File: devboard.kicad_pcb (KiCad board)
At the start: 2 copper layers, 0 parts

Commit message: Exploration into bus layout
This commit made to save progress before attempting new layout.
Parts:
- added C1: 100n, Capacitor_SMD:C_0603_1608Metric_Pad1.08x0.95mm_HandSolder, F.Cu at (166.4, 105.4)
- added C10: 10u, Capacitor_SMD:C_0603_1608Metric_Pad1.08x0.95mm_HandSolder, F.Cu at (187.1, 76.6)
- added C11: 100n, Capacitor_SMD:C_0603_1608Metric_Pad1.08x0.95mm_HandSolder, F.Cu at (43.2, 31.3)
- added C12: 100n, Capacitor_SMD:C_0603_1608Metric_Pad1.08x0.95mm_HandSolder, F.Cu at (268.0, 146.3)
- added C13: 100n, Capacitor_SMD:C_0603_1608Metric_Pad1.08x0.95mm_HandSolder, F.Cu at (61.6, 32.2)
- added C14: 100n, Capacitor_SMD:C_0603_1608Metric_Pad1.08x0.95mm_HandSolder, F.Cu at (287.0, 146.9)
- added C15: 100n, Capacitor_SMD:C_0603_1608Metric_Pad1.08x0.95mm_HandSolder, F.Cu at (68.6, 31.3)
- added C16: 100n, Capacitor_SMD:C_0603_1608Metric_Pad1.08x0.95mm_HandSolder, F.Cu at (293.4, 146.3)
- added C17: 100n, Capacitor_SMD:C_0603_1608Metric_Pad1.08x0.95mm_HandSolder, F.Cu at (87.0, 32.2)
- added C18: 100n, Capacitor_SMD:C_0603_1608Metric_Pad1.08x0.95mm_HandSolder, F.Cu at (312.4, 146.7)
- added C19: 100n, Capacitor_SMD:C_0603_1608Metric_Pad1.08x0.95mm_HandSolder, F.Cu at (92.7, 31.5)
- added C2: 100n, Capacitor_SMD:C_0603_1608Metric_Pad1.08x0.95mm_HandSolder, F.Cu at (144.8, 123.7)
- added C20: 100n, Capacitor_SMD:C_0603_1608Metric_Pad1.08x0.95mm_HandSolder, F.Cu at (318.1, 146.7)
- added C21: 100n, Capacitor_SMD:C_0603_1608Metric_Pad1.08x0.95mm_HandSolder, F.Cu at (111.8, 32.2)
- added C22: 100n, Capacitor_SMD:C_0603_1608Metric_Pad1.08x0.95mm_HandSolder, F.Cu at (337.2, 146.7)
- added C23: 100n, Capacitor_SMD:C_0603_1608Metric_Pad1.08x0.95mm_HandSolder, F.Cu at (188.1, 91.6)
- added C24: 10u, Capacitor_SMD:C_0603_1608Metric_Pad1.08x0.95mm_HandSolder, F.Cu at (183.7, 96.3)
- added C25: 10n, Capacitor_SMD:C_0603_1608Metric_Pad1.08x0.95mm_HandSolder, F.Cu at (170.7, 108.4)
- added C26: 100n, Capacitor_SMD:C_0603_1608Metric_Pad1.08x0.95mm_HandSolder, F.Cu at (144.8, 121.2)
- added C27: 100n, Capacitor_SMD:C_0603_1608Metric_Pad1.08x0.95mm_HandSolder, F.Cu at (154.0, 118.5)
- added C28: 100n, Capacitor_SMD:C_0603_1608Metric_Pad1.08x0.95mm_HandSolder, F.Cu at (183.7, 88.7)
- added C3: 100n, Capacitor_SMD:C_0603_1608Metric_Pad1.08x0.95mm_HandSolder, F.Cu at (149.1, 121.2)
- added C4: 100n, Capacitor_SMD:C_0603_1608Metric_Pad1.08x0.95mm_HandSolder, F.Cu at (186.8, 81.6)
- added C5: 1u, Capacitor_SMD:C_0603_1608Metric_Pad1.08x0.95mm_HandSolder, F.Cu at (158.8, 81.9)
- added C6: 1u, Capacitor_SMD:C_0603_1608Metric_Pad1.08x0.95mm_HandSolder, F.Cu at (157.0, 109.8)
- added C7: 100n, Capacitor_SMD:C_0603_1608Metric_Pad1.08x0.95mm_HandSolder, F.Cu at (183.7, 86.2)
- added C8: 10u, Capacitor_SMD:C_0603_1608Metric_Pad1.08x0.95mm_HandSolder, F.Cu at (157.0, 107.3)
- added C9: 10u, Capacitor_SMD:C_0603_1608Metric_Pad1.08x0.95mm_HandSolder, F.Cu at (187.1, 79.1)
- added D1: 3.3 VRW, Diode_SMD:D_SOD-923, F.Cu at (191.6, 89.9)
- added D10: 3.3 VRW, Diode_SMD:D_SOD-923, F.Cu at (190.7, 76.3)
- added D2: RXLED, LED_SMD:LED_0603_1608Metric_Castellated, F.Cu at (104.8, 124.0)
- added D3: 3.3 VRW, Diode_SMD:D_SOD-923, F.Cu at (191.6, 88.0)
- added D4: 3.3 VRW, Diode_SMD:D_SOD-923, F.Cu at (191.6, 86.0)
- added D5: TXLED, LED_SMD:LED_0603_1608Metric_Castellated, F.Cu at (112.0, 101.3)
- added D6: 3.3 VRW, Diode_SMD:D_SOD-923, F.Cu at (191.6, 84.1)
- added D7: 3.3 VRW, Diode_SMD:D_SOD-923, F.Cu at (191.6, 82.1)
- added D8: 3.3 VRW, Diode_SMD:D_SOD-923, F.Cu at (190.7, 80.2)
- added D9: 3.3 VRW, Diode_SMD:D_SOD-923, F.Cu at (190.7, 78.2)
- added FB1: 500mA, Inductor_SMD:L_0603_1608Metric_Pad1.05x0.95mm_HandSolder, F.Cu at (171.0, 100.9)
- added J1: Conn_01x04, Connector_PinHeader_2.54mm:PinHeader_1x04_P2.54mm_Vertical, F.Cu at (147.7, 97.6)
- added J2: Conn_02x05_Odd_Even, Connector_PinHeader_1.27mm:PinHeader_2x05_P1.27mm_Vertical, F.Cu at (129.9, 116.9)
- added J3: USB_B_Micro, Connector_USB:USB_Micro-B_Wuerth_629105150521, F.Cu at (69.8, 163.8)
- added J4: Conn_01x04, Connector_PinHeader_2.54mm:PinHeader_1x04_P2.54mm_Vertical, F.Cu at (173.3, 77.6)
- added J5: Conn_02x10_Counter_Clockwise, Connector_PinHeader_2.54mm:PinHeader_2x10_P2.54mm_Vertical, F.Cu at (19.1, 66.0)
- added J6: Conn_02x04_Counter_Clockwise, Connector_PinHeader_2.54mm:PinHeader_2x04_P2.54mm_Vertical, F.Cu at (154.9, 96.1)
- added Q1: Q_NPN_BEC, Package_TO_SOT_SMD:SOT-23, F.Cu at (162.0, 105.3)
- added Q2: Q_NPN_BEC, Package_TO_SOT_SMD:SOT-23, F.Cu at (166.6, 101.9)
- added R1: 330, Resistor_SMD:R_0603_1608Metric_Pad0.98x0.95mm_HandSolder, F.Cu at (161.4, 108.9)
- added R10: 40k, Resistor_SMD:R_0603_1608Metric_Pad0.98x0.95mm_HandSolder, F.Cu at (269.9, 149.9)
- added R11: 1k, Resistor_SMD:R_0603_1608Metric_Pad0.98x0.95mm_HandSolder, F.Cu at (162.7, 121.4)
- added R12: 40k, Resistor_SMD:R_0603_1608Metric_Pad0.98x0.95mm_HandSolder, F.Cu at (269.9, 142.6)
- added R13: 40k, Resistor_SMD:R_0603_1608Metric_Pad0.98x0.95mm_HandSolder, F.Cu at (87.0, 24.5)
- added R14: 40k, Resistor_SMD:R_0603_1608Metric_Pad0.98x0.95mm_HandSolder, F.Cu at (312.4, 139.1)
- added R15: 40k, Resistor_SMD:R_0603_1608Metric_Pad0.98x0.95mm_HandSolder, F.Cu at (70.5, 34.9)
- added R16: 40k, Resistor_SMD:R_0603_1608Metric_Pad0.98x0.95mm_HandSolder, F.Cu at (295.3, 149.9)
- added R17: 40k, Resistor_SMD:R_0603_1608Metric_Pad0.98x0.95mm_HandSolder, F.Cu at (61.6, 28.3)
- added R18: 40k, Resistor_SMD:R_0603_1608Metric_Pad0.98x0.95mm_HandSolder, F.Cu at (287.0, 143.2)
- added R19: 40k, Resistor_SMD:R_0603_1608Metric_Pad0.98x0.95mm_HandSolder, F.Cu at (111.8, 24.5)
- added R2: 10k, Resistor_SMD:R_0603_1608Metric_Pad0.98x0.95mm_HandSolder, F.Cu at (149.6, 118.5)
- added R20: 40k, Resistor_SMD:R_0603_1608Metric_Pad0.98x0.95mm_HandSolder, F.Cu at (337.2, 139.1)
- added R21: 40k, Resistor_SMD:R_0603_1608Metric_Pad0.98x0.95mm_HandSolder, F.Cu at (94.6, 35.2)
- added R22: 40k, Resistor_SMD:R_0603_1608Metric_Pad0.98x0.95mm_HandSolder, F.Cu at (320.0, 150.1)
- added R23: 40k, Resistor_SMD:R_0603_1608Metric_Pad0.98x0.95mm_HandSolder, F.Cu at (70.5, 27.6)
- added R24: 40k, Resistor_SMD:R_0603_1608Metric_Pad0.98x0.95mm_HandSolder, F.Cu at (295.3, 142.6)
- added R25: 40k, Resistor_SMD:R_0603_1608Metric_Pad0.98x0.95mm_HandSolder, F.Cu at (87.0, 28.2)
- added R26: 40k, Resistor_SMD:R_0603_1608Metric_Pad0.98x0.95mm_HandSolder, F.Cu at (312.4, 142.9)
- added R27: 40k, Resistor_SMD:R_0603_1608Metric_Pad0.98x0.95mm_HandSolder, F.Cu at (94.6, 27.6)
- added R28: 40k, Resistor_SMD:R_0603_1608Metric_Pad0.98x0.95mm_HandSolder, F.Cu at (320.0, 142.9)
- added R29: 40k, Resistor_SMD:R_0603_1608Metric_Pad0.98x0.95mm_HandSolder, F.Cu at (111.8, 28.3)
- added R3: 10k, Resistor_SMD:R_0603_1608Metric_Pad0.98x0.95mm_HandSolder, F.Cu at (154.0, 115.9)
- added R30: 40k, Resistor_SMD:R_0603_1608Metric_Pad0.98x0.95mm_HandSolder, F.Cu at (337.2, 142.9)
- added R31: 4.7k, Resistor_SMD:R_0603_1608Metric_Pad0.98x0.95mm_HandSolder, F.Cu at (109.2, 124.0)
- added R32: 4.7k, Resistor_SMD:R_0603_1608Metric_Pad0.98x0.95mm_HandSolder, F.Cu at (167.0, 112.9)
- added R4: 10k, Resistor_SMD:R_0603_1608Metric_Pad0.98x0.95mm_HandSolder, F.Cu at (157.8, 122.3)
- added R5: 40k, Resistor_SMD:R_0603_1608Metric_Pad0.98x0.95mm_HandSolder, F.Cu at (45.1, 27.6)
- added R6: 1k, Resistor_SMD:R_0603_1608Metric_Pad0.98x0.95mm_HandSolder, F.Cu at (167.0, 115.5)
- added R7: 40k, Resistor_SMD:R_0603_1608Metric_Pad0.98x0.95mm_HandSolder, F.Cu at (61.6, 24.5)
- added R8: 40k, Resistor_SMD:R_0603_1608Metric_Pad0.98x0.95mm_HandSolder, F.Cu at (287.0, 139.4)
- added R9: 40k, Resistor_SMD:R_0603_1608Metric_Pad0.98x0.95mm_HandSolder, F.Cu at (45.1, 34.9)
- added SW1: SW_SPST, Button_Switch_SMD:SW_SPST_PTS810, F.Cu at (113.2, 97.7)
- added TP1: TestPoint, Connector_PinHeader_2.54mm:PinHeader_1x01_P2.54mm_Vertical, F.Cu at (135.6, 122.2)
- added TP10: TestPoint, Connector_PinHeader_2.54mm:PinHeader_1x01_P2.54mm_Vertical, F.Cu at (152.5, 108.3)
- added TP11: TestPoint, Connector_PinHeader_2.54mm:PinHeader_1x01_P2.54mm_Vertical, F.Cu at (178.0, 77.6)
- added TP2: TestPoint, Connector_PinHeader_2.54mm:PinHeader_1x01_P2.54mm_Vertical, F.Cu at (166.7, 96.1)
- added TP3: TestPoint, Connector_PinHeader_2.54mm:PinHeader_1x01_P2.54mm_Vertical, F.Cu at (145.1, 117.6)
- added TP4: TestPoint, Connector_PinHeader_2.54mm:PinHeader_1x01_P2.54mm_Vertical, F.Cu at (162.1, 100.7)
- added TP5: TestPoint, Connector_PinHeader_2.54mm:PinHeader_1x01_P2.54mm_Vertical, F.Cu at (162.1, 96.1)
- added TP6: TestPoint, Connector_PinHeader_2.54mm:PinHeader_1x01_P2.54mm_Vertical, F.Cu at (182.6, 77.6)
- added TP7: TestPoint, Connector_PinHeader_2.54mm:PinHeader_1x01_P2.54mm_Vertical, F.Cu at (140.3, 122.2)
- added TP8: TestPoint, Connector_PinHeader_2.54mm:PinHeader_1x01_P2.54mm_Vertical, F.Cu at (178.0, 82.3)
- added TP9: TestPoint, Connector_PinHeader_2.54mm:PinHeader_1x01_P2.54mm_Vertical, F.Cu at (140.5, 117.6)
- added U1: ATmega128L-8AU, Package_QFP:TQFP-64_14x14mm_P0.8mm, F.Cu at (128.9, 44.5)
- added U10: FT232RL, Package_SO:SSOP-28_5.3x10.2mm_P0.65mm, F.Cu at (69.8, 154.9)
- added U2: MAX6371, Package_TO_SOT_SMD:SOT-23-8, F.Cu at (147.8, 109.8)
- added U3: CY62158EV30LL-45ZSXIT, Package_SO:TSOP-II-44_10.16x18.41mm_P0.8mm, F.Cu at (278.6, 146.8)
- added U4: AP2112K-3.3, Package_TO_SOT_SMD:SOT-23-5, F.Cu at (135.7, 117.6)
- added U5: CY62158EV30LL-45ZSXIT, Package_SO:TSOP-II-44_10.16x18.41mm_P0.8mm, F.Cu at (53.5, 31.7)
- added U6: CY62158EV30LL-45ZSXIT, Package_SO:TSOP-II-44_10.16x18.41mm_P0.8mm, F.Cu at (78.7, 31.8)
- added U7: CY62158EV30LL-45ZSXIT, Package_SO:TSOP-II-44_10.16x18.41mm_P0.8mm, F.Cu at (304.2, 146.7)
- added U8: CY62158EV30LL-45ZSXIT, Package_SO:TSOP-II-44_10.16x18.41mm_P0.8mm, F.Cu at (103.5, 31.8)
- added U9: CY62158EV30LL-45ZSXIT, Package_SO:TSOP-II-44_10.16x18.41mm_P0.8mm, F.Cu at (328.9, 146.7)
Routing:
- net /IO4: track 0.00 -> 73.3 mm, vias 0 -> 3
- net /A9: track 0.00 -> 69.0 mm, vias 0 -> 3
- net /A10: track 0.00 -> 66.5 mm, vias 0 -> 3
- net /A11: track 0.00 -> 65.1 mm, vias 0 -> 3
- net /A12: track 0.00 -> 63.4 mm, vias 0 -> 3
- net /A13: track 0.00 -> 62.5 mm, vias 0 -> 3
- net /A19: track 0.00 -> 62.0 mm
- net /A18: track 0.00 -> 61.4 mm
- net /A17: track 0.00 -> 60.8 mm
- net /A16: track 0.00 -> 60.2 mm
- net /A15: track 0.00 -> 59.6 mm
- net /A14: track 0.00 -> 59.5 mm, vias 0 -> 3
- net /IO0: track 0.00 -> 35.8 mm
- net /A0: track 0.00 -> 31.8 mm
- net /A1: track 0.00 -> 29.7 mm
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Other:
- copper layers 2 -> 4

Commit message: Successfully route memories
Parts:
- removed R13, R14, R15, R16, R19, R20, R21, R22: 40k, Resistor_SMD:R_0603_1608Metric_Pad0.98x0.95mm_HandSolder
- moved U3 247.4 mm to (47.1, 59.6)
- moved R12 247.0 mm to (38.7, 55.5)
- moved R24 247.0 mm to (64.1, 55.5)
- moved R10 247.0 mm to (38.7, 62.8), turned to 270 degrees
- moved C12 245.2 mm to (38.7, 59.3)
- moved C16 245.2 mm to (64.1, 59.3)
- moved U7 245.2 mm to (74.9, 59.7)
- moved R8 244.6 mm to (58.4, 52.4)
- moved R18 244.6 mm to (58.4, 56.2)
- moved C14 244.5 mm to (58.4, 60.1)
- moved R28 244.1 mm to (92.1, 55.5)
- moved C20 242.3 mm to (92.1, 59.4)
- moved R26 242.1 mm to (86.4, 56.1)
- moved C18 242.1 mm to (86.4, 60.1)
- moved U9 241.9 mm to (103.1, 59.7)
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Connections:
- R10 pad 1: /~WE -> Net-(R10-Pad1)
- R10 pad 2: Net-(C10-Pad1) -> /~WE
- R7 pad 1: /~OE -> Net-(C11-Pad1)
- R7 pad 2: Net-(C11-Pad1) -> /~OE
- R8 pad 1: /~OE -> Net-(R8-Pad1)
- R8 pad 2: Net-(C10-Pad1) -> /~OE
- R9 pad 1: /~WE -> Net-(C11-Pad1)
- R9 pad 2: Net-(C11-Pad1) -> /~WE
- U1 pad 2: Net-(U1-Pad2) -> /~OE
- U1 pad 3: Net-(U1-Pad3) -> /~WE
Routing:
- net GND: track 29.4 -> 187.5 mm, vias 0 -> 28
- net /IO1: track 2.92 -> 143.7 mm
- net /IO2: track 0.00 -> 137.4 mm
- net /IO3: track 0.00 -> 136.3 mm
- net /A8: track 0.00 -> 132.9 mm, vias 0 -> 6
- net /IO7: track 0.00 -> 132.5 mm, vias 0 -> 6
- net /IO6: track 0.00 -> 131.1 mm, vias 0 -> 6
- net /A5: track 0.00 -> 130.1 mm, vias 0 -> 6
- net /A6: track 0.00 -> 127.3 mm, vias 0 -> 6
- net /IO5: track 0.00 -> 126.7 mm, vias 0 -> 6
- net /A7: track 0.00 -> 124.4 mm, vias 0 -> 6
- net /~WE: track 19.1 -> 135.6 mm
- net /IO0: track 35.8 -> 142.4 mm
- net /A1: track 29.7 -> 126.2 mm
- net /A2: track 29.4 -> 125.0 mm
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- added copper zone on In2.Cu, net GND

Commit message: Join memory busses
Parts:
- moved U1 11.0 mm to (144.8, 47.0)
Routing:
- net (no net): track 67.5 -> 0.00 mm
- net Net-(C10-Pad1): track 6.20 -> 58.0 mm
- net /A17: track 126.7 -> 176.7 mm, vias 0 -> 2
- net /A18: track 127.5 -> 176.8 mm, vias 0 -> 2
- net /A19: track 129.3 -> 177.9 mm, vias 0 -> 2
- net /A16: track 125.5 -> 173.9 mm, vias 0 -> 2
- net /IO3: track 136.3 -> 184.4 mm, vias 0 -> 2
- net /IO1: track 143.7 -> 191.1 mm, vias 0 -> 2
- net /A15: track 124.3 -> 170.9 mm, vias 0 -> 2
- net /IO0: track 142.4 -> 189.0 mm, vias 0 -> 2
- net /A0: track 127.3 -> 172.9 mm, vias 0 -> 2
- net /A1: track 126.2 -> 171.0 mm, vias 0 -> 2
- net /A2: track 125.0 -> 169.1 mm, vias 0 -> 2
- net /A3: track 123.9 -> 167.2 mm, vias 0 -> 2
- net /A4: track 122.7 -> 164.4 mm, vias 0 -> 2
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
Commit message: Routing almost complete
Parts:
- removed C7: 100n, Capacitor_SMD:C_0603_1608Metric_Pad1.08x0.95mm_HandSolder
- removed C8: 10u, Capacitor_SMD:C_0603_1608Metric_Pad1.08x0.95mm_HandSolder
- moved D3 161.9 mm to (44.7, 19.8), turned to 90 degrees
- moved J3 151.0 mm to (164.6, 46.2), turned to 90 degrees
- moved D7 150.7 mm to (44.7, 48.5), turned to 270 degrees
- moved TP1 138.2 mm to (42.3, 20.3), turned to 180 degrees
- moved U10 137.5 mm to (153.7, 46.0), turned to 0 degrees
- moved D4 135.8 mm to (72.6, 20.6), turned to 270 degrees
- moved TP4 130.8 mm to (42.3, 48.2)
- moved J5 123.5 mm to (142.5, 70.1), turned to 90 degrees
- moved TP2 122.9 mm to (70.1, 20.2)
- moved R32 100.2 mm to (119.4, 24.8), turned to 180 degrees
- moved D2 97.9 mm to (152.7, 38.6), turned to 90 degrees
- moved TP3 90.6 mm to (148.8, 27.0)
- moved D9 90.1 mm to (100.8, 70.9), turned to 90 degrees
- moved C3 89.9 mm to (123.7, 34.9), turned to 90 degrees
- moved J2 89.0 mm to (133.3, 27.9), turned to 90 degrees
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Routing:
- net /A0: track 172.9 -> 264.5 mm, vias 2 -> 5
- net /A1: track 171.0 -> 259.8 mm, vias 2 -> 5
- net /A2: track 169.1 -> 241.4 mm, vias 2 -> 4
- net /A3: track 167.2 -> 234.8 mm, vias 2 -> 4
- net /A12: track 133.3 -> 191.8 mm, vias 6 -> 9
- net /A14: track 123.0 -> 178.7 mm, vias 6 -> 9
- net /A13: track 127.0 -> 182.2 mm, vias 6 -> 9
- net /IO3: track 184.4 -> 239.5 mm, vias 2 -> 5
- net GND: track 169.4 -> 224.6 mm, vias 24 -> 50
- net /A4: track 164.4 -> 215.0 mm, vias 2 -> 3
- net /IO1: track 191.1 -> 241.4 mm, vias 2 -> 5
- net /A11: track 136.5 -> 185.7 mm, vias 6 -> 7
- net /IO0: track 189.0 -> 237.3 mm, vias 2 -> 5
- net /IO2: track 137.4 -> 185.0 mm, vias 0 -> 2
- net /A10: track 142.2 -> 189.5 mm, vias 6 -> 7
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- added copper zone on In1.Cu, net VCC
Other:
- net class Default: via_dia 0.8 -> 0.6; via_drill 0.4 -> 0.3
- board text added: ""If I have seen further, it is by standing upon the shoulders of giants""
- board text added: "DaVinci Payload Two"
- board text added: "Daniel Avishai Stutman - 2021"

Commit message: Autorouting pass
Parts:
- moved TP5 58.7 mm to (70.2, 48.2), turned to 0 degrees
- moved D8 56.5 mm to (72.6, 48.7), turned to 270 degrees
- moved TP3 50.7 mm to (98.5, 20.4)
- moved D6 50.7 mm to (101.1, 20.8)
- moved TP7 24.4 mm to (128.3, 24.1)
- moved J2 3.42 mm to (132.1, 24.8)
- moved J6 1.57 mm to (165.7, 59.7)
- moved TP11 1.40 mm to (164.5, 32.4)
- moved D3 0.84 mm to (44.7, 20.7), turned to 270 degrees
- moved J1 0.64 mm to (146.3, 59.3)
- moved U2 0.51 mm to (122.0, 41.8)
- moved J5 0.46 mm to (142.2, 70.5)
- moved TP10 0.33 mm to (120.4, 38.0)
- moved TP8 0.28 mm to (121.0, 34.3)
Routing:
- net /~OE: track 11.7 -> 202.2 mm, vias 0 -> 12
- net /M1_CE2: track 6.08 -> 152.7 mm, vias 0 -> 4
- net /M4_CE2: track 6.08 -> 115.1 mm, vias 0 -> 3
- net /A17: track 203.8 -> 297.0 mm, vias 3 -> 7
- net /M2_CE2: track 6.16 -> 90.7 mm, vias 0 -> 6
- net Net-(C10-Pad1): track 58.0 -> 137.4 mm, vias 0 -> 5
- net /A6: track 171.4 -> 250.8 mm, vias 7 -> 11
- net /A9: track 191.5 -> 267.1 mm, vias 7 -> 8
- net /M6_CE2: track 3.26 -> 77.4 mm, vias 0 -> 2
- net /A11: track 185.7 -> 257.6 mm, vias 7 -> 9
- net /A16: track 202.4 -> 273.5 mm, vias 3 -> 4
- net /A8: track 177.6 -> 245.2 mm, vias 7 -> 9
- net /~RST: track 20.9 -> 88.2 mm, vias 0 -> 4
- net /IO4: track 162.9 -> 229.2 mm, vias 7 -> 9
- net /A10: track 189.5 -> 255.3 mm, vias 7 -> 9
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
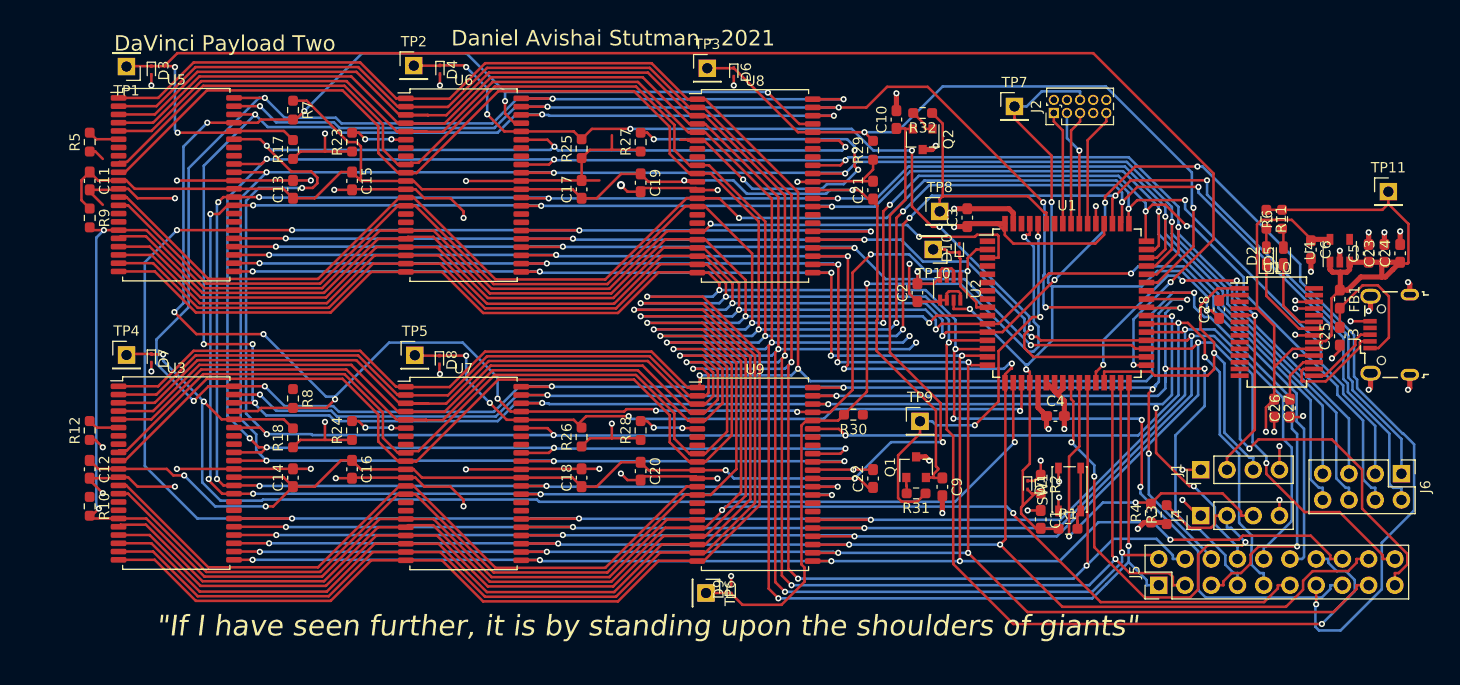
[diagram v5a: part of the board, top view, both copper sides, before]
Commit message: Improve silk
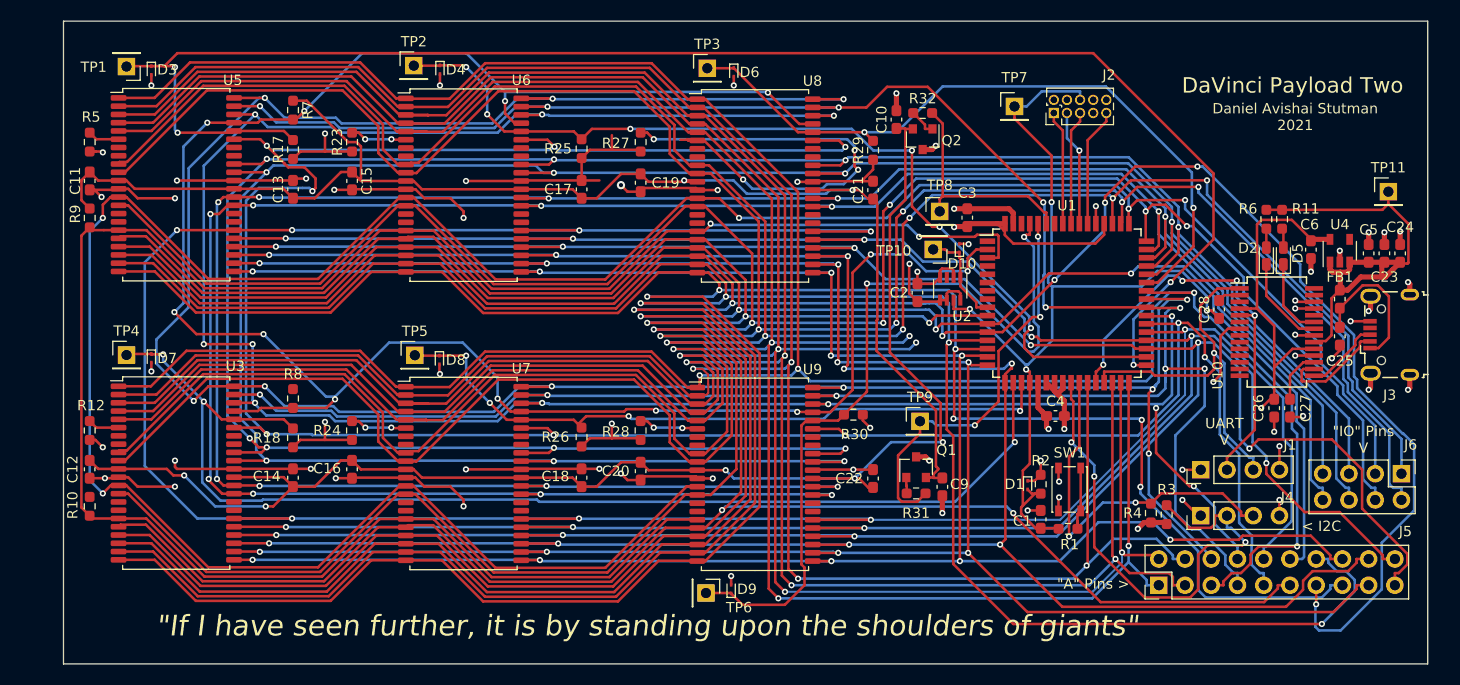
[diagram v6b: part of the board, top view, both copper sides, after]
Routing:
- net /IO2: track 225.8 -> 257.8 mm, vias 3 -> 5
- net GND: track 238.0 -> 245.0 mm, vias 58 -> 63
- net VCC: track 81.7 -> 79.8 mm
- net /A15: track 260.7 -> 262.0 mm
- net /A16: track 273.5 -> 274.4 mm
- net /A17: track 297.0 -> 297.9 mm
- net /IO1: track 289.1 -> 288.4 mm
- net /A2: track 254.0 -> 254.7 mm
- net /IO6: track 236.5 -> 237.0 mm
- net /~WE: track 198.4 -> 198.5 mm, vias 4 -> 2
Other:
- board outline added: 132.1 x 62.2 mm
- board text added: ""A" Pins >"
- board text added: ""IO" Pins V"
- board text added: "< I2C"
- board text added: "DEVELOPMENT BOARD NOT FOR FLIGHT"
- board text added: "Daniel Avishai Stutman 2021"
- board text added: "UART V"
- board text removed: "Daniel Avishai Stutman - 2021"
